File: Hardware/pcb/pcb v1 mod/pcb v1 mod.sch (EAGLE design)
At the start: 41 parts, among them J1 AVR_SPI_PRG_6PTH, Q1 2N3906, U1 ADP3338AKCZ-3.3RL7, U2 ATMEGA328P, Y1 16Mhz

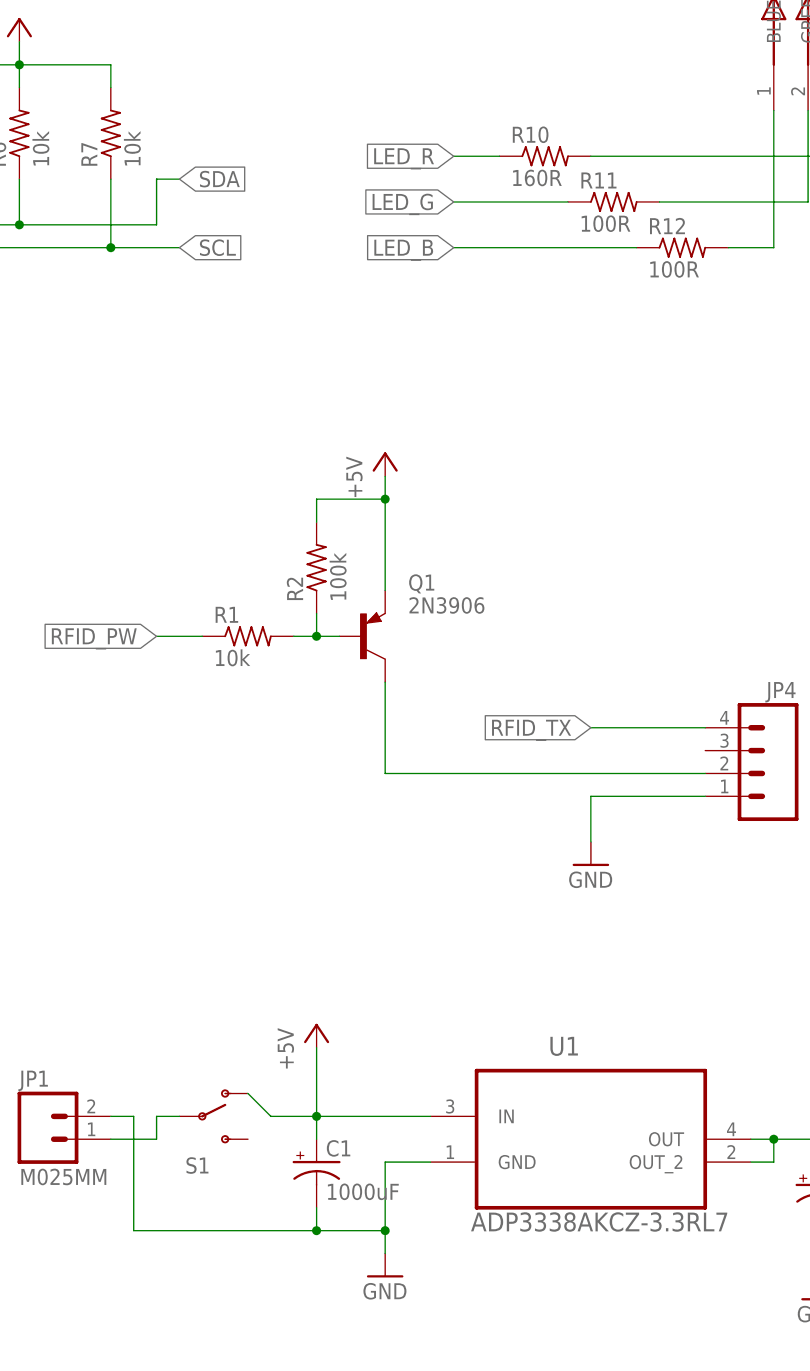
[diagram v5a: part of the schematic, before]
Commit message: cambio resistencia led
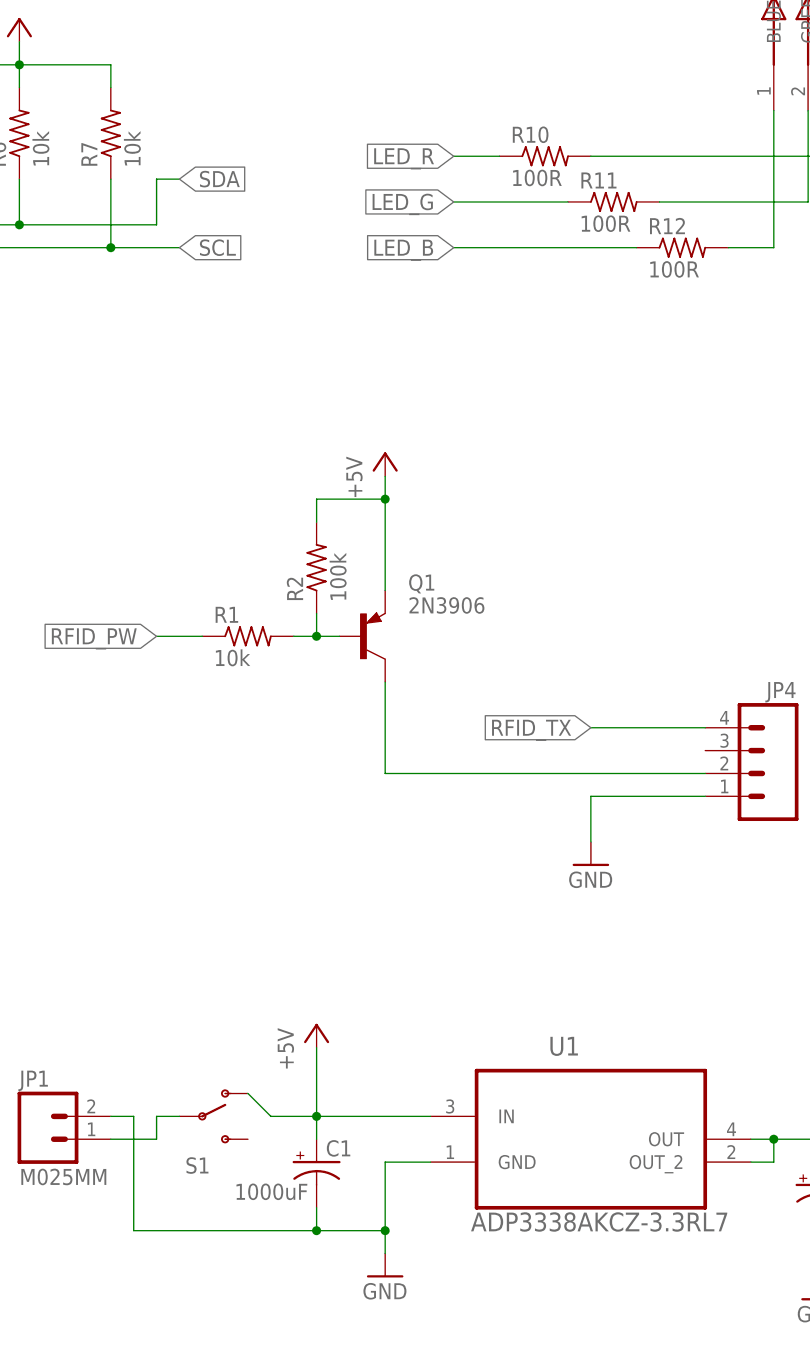
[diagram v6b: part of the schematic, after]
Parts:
- R10: value 160R -> 100R
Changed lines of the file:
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@@
 <part name="JP3" library="SparkFun-Connectors" deviceset="M03" device="PTH"/>
 <part name="JP7" library="SparkFun-Connectors" deviceset="M03" device="PTH"/>
-<part name="R10" library="rcl" deviceset="R-US_" device="R1206" value="160R"/>
+<part name="R10" library="rcl" deviceset="R-US_" device="R1206" value="100R"/>
 <part name="R11" library="rcl" deviceset="R-US_" device="R0805" value="100R"/>
 <part name="R12" library="rcl" deviceset="R-US_" device="R0805" value="100R"/>
@@
 </instance>
 <instance part="R1" gate="G$1" x="243.84" y="86.36"/>
-<instance part="C1" gate="G$1" x="251.46" y="27.94"/>
+<instance part="C1" gate="G$1" x="251.46" y="27.94" smashed="yes">
+<attribute name="NAME" x="252.476" y="28.575" size="1.778" layer="95"/>
+<attribute name="VALUE" x="242.316" y="23.749" size="1.778" layer="96"/>
+</instance>
 <instance part="C2" gate="G$1" x="307.34" y="25.4"/>
 <instance part="C10" gate="G$1" x="187.96" y="83.82"/>

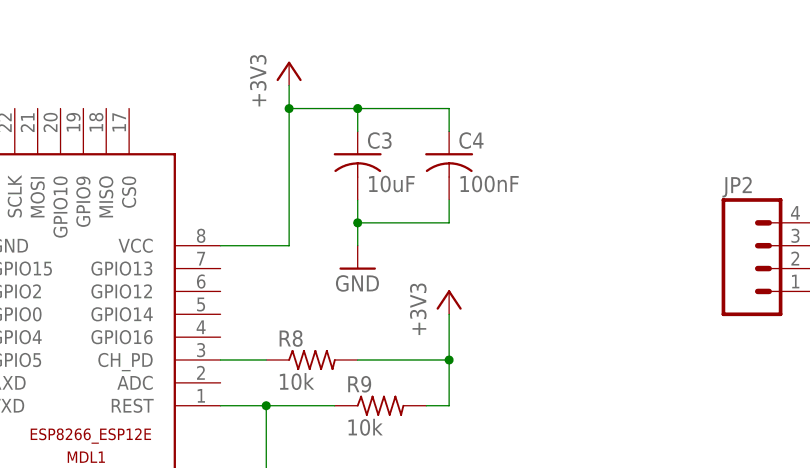
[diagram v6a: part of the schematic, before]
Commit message: Cambio valor C3
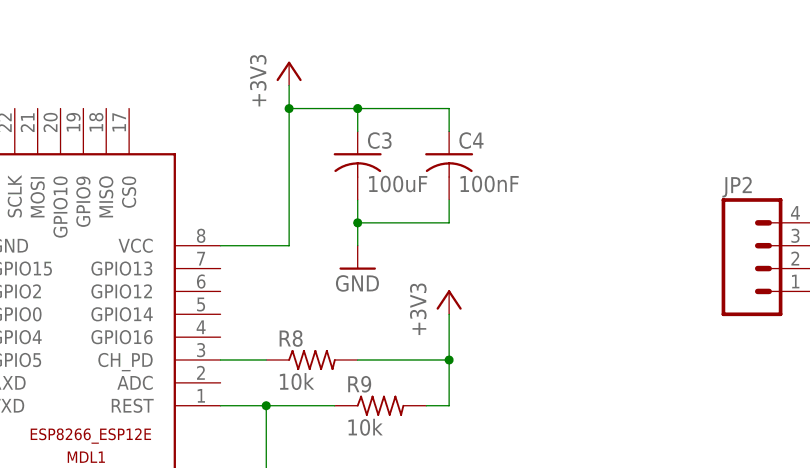
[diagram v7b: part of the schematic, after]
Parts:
- C3: value 10uF -> 100uF
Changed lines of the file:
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@@
 <part name="R12" library="rcl" deviceset="R-US_" device="R0805" value="100R"/>
 <part name="GND10" library="supply1" deviceset="GND" device=""/>
-<part name="C3" library="rcl" deviceset="C-US" device="C1206" value="10uF"/>
+<part name="C3" library="rcl" deviceset="C-US" device="C1206" value="100uF"/>
 <part name="C4" library="rcl" deviceset="C-US" device="C0805" value="100nF"/>
 <part name="GND9" library="supply1" deviceset="GND" device=""/>
